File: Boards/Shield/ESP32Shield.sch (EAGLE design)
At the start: 29 parts, among them Q1 220mA/50V/3.5Ω, U1 5V

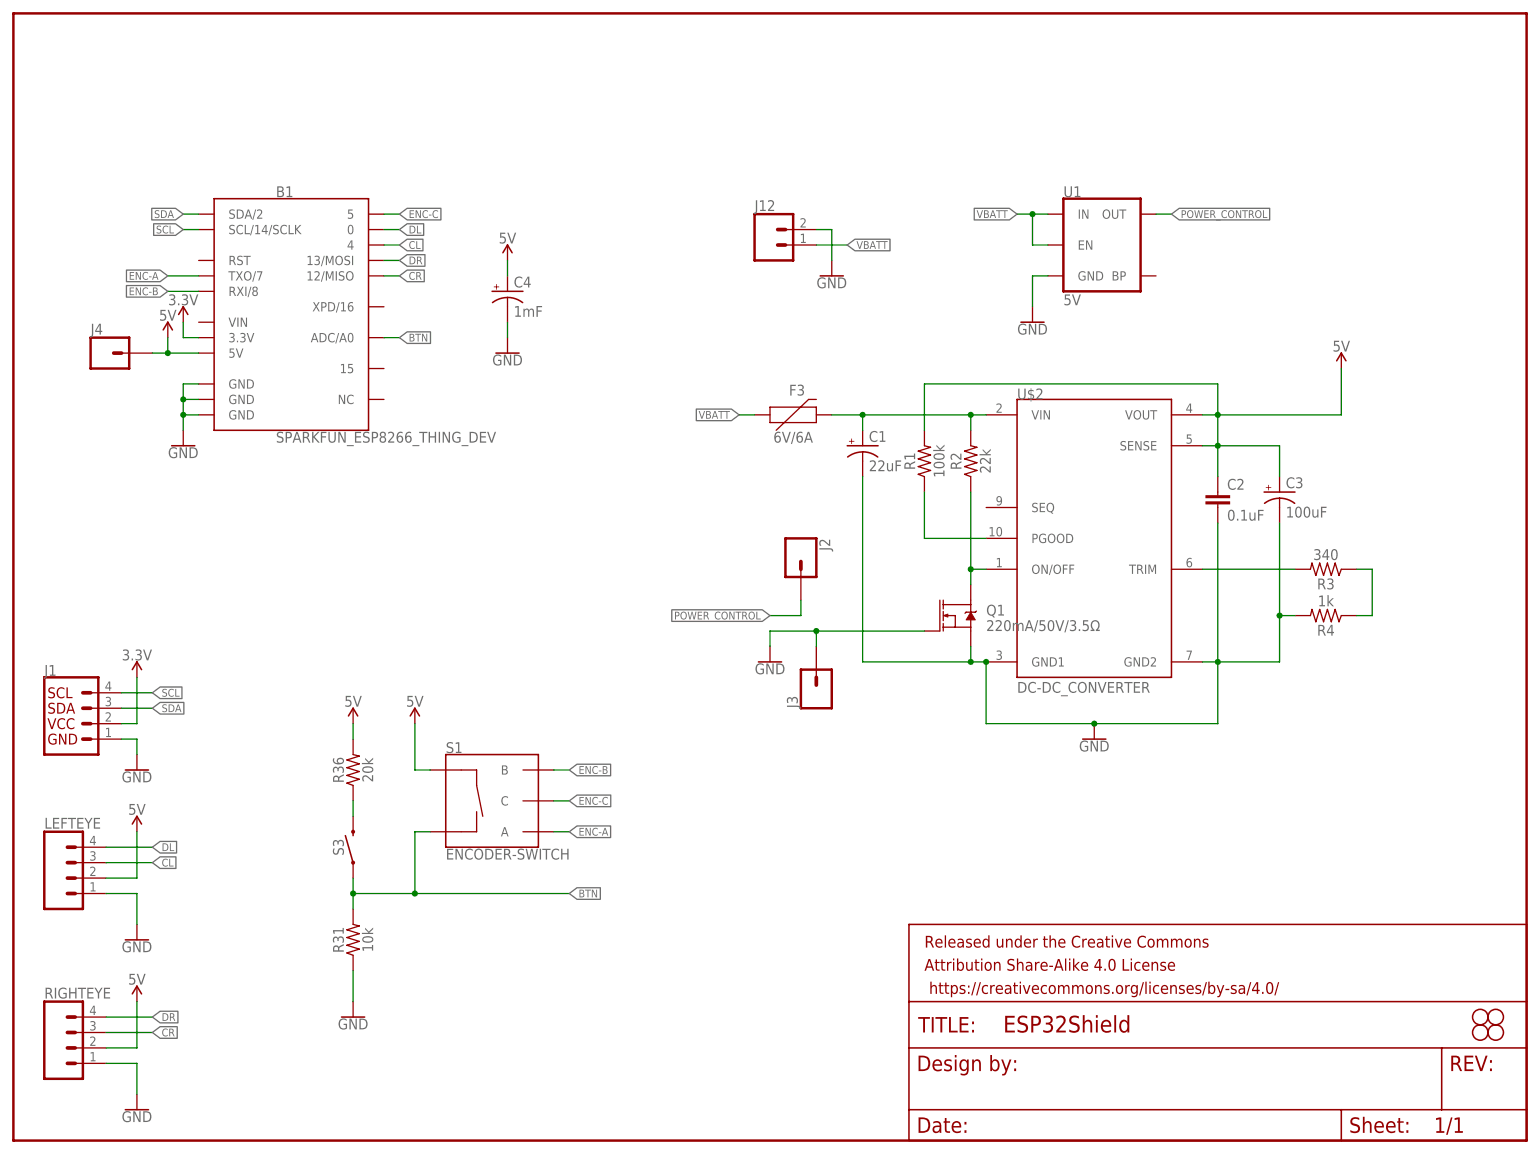
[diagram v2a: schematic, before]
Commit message: finished ESP32 Shield layout
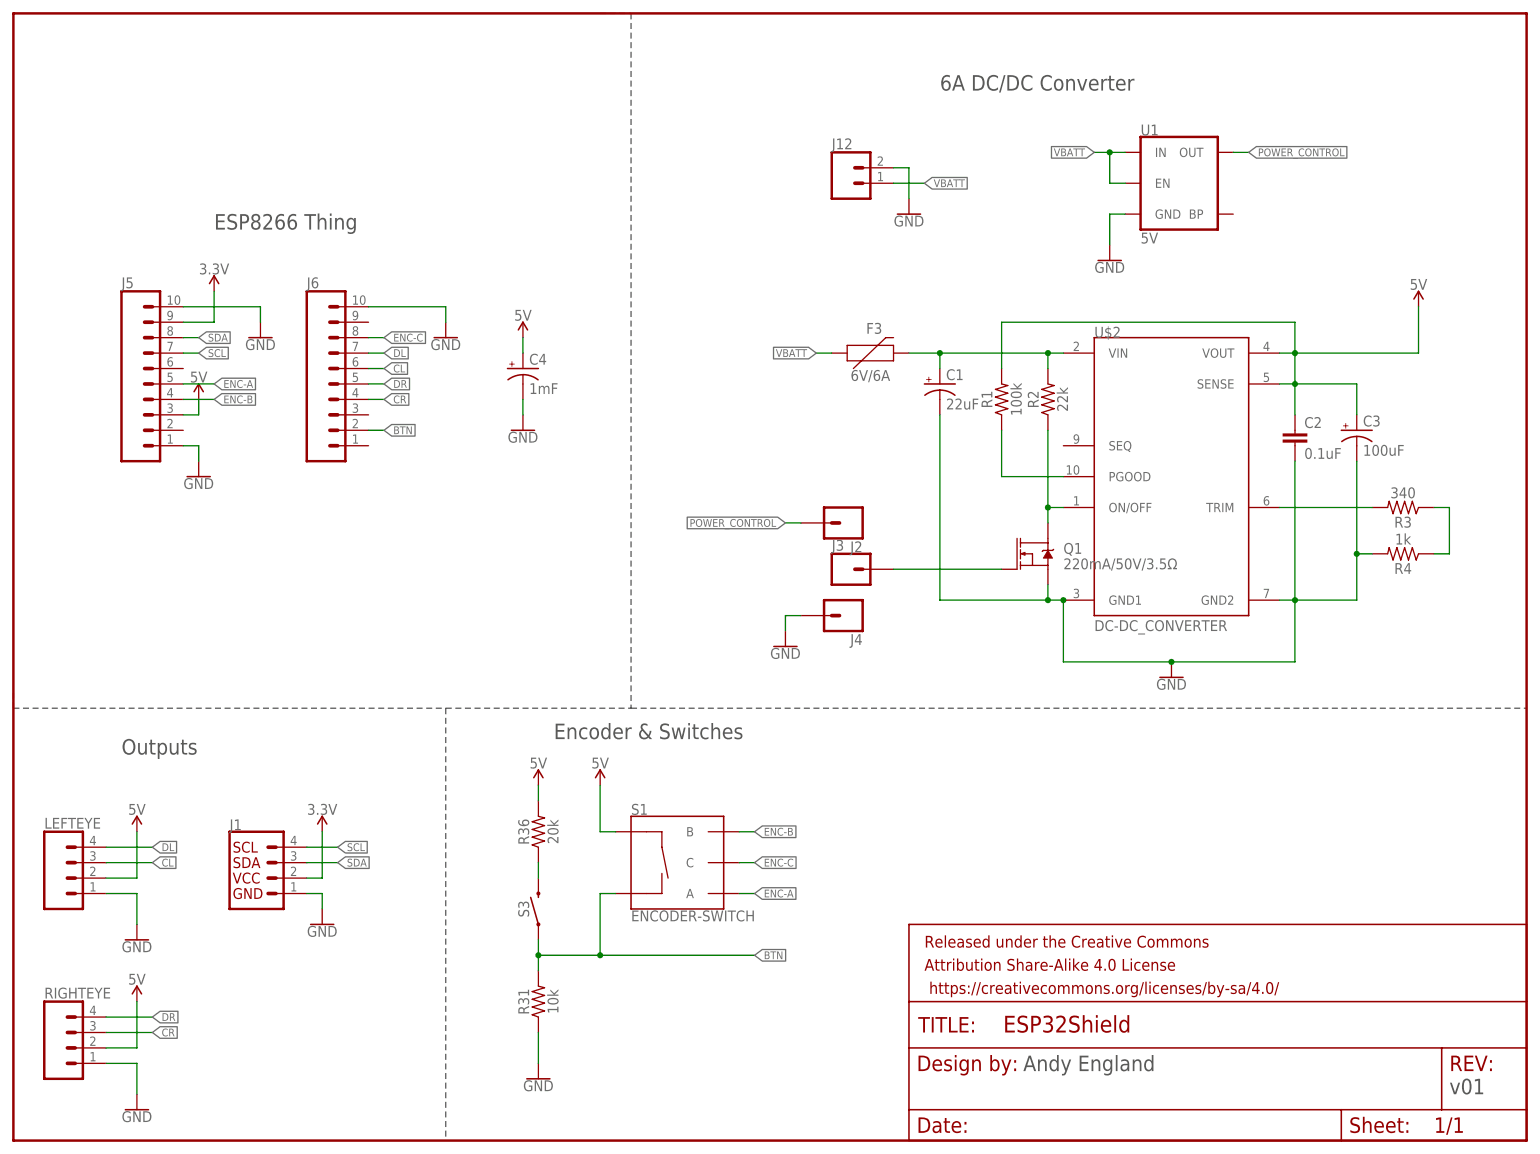
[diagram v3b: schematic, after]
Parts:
- removed B1: SPARKFUN_ESP8266_THING_DEV, SparkFun-Boards:SPARKFUN_ESP8266_THING_DEV
- removed H3, H4, H5, H6: STAND-OFFTIGHT, SparkFun-Hardware:STAND-OFFTIGHT
- added J5, J6: (no value), SparkFun-Connectors:CONN_10NO_SILK_PTH_FEMALE
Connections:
- new net N$1: J3.1, Q1.G
- net 3.3V: now also J5.9; no longer B1.3.3V
- net 5V: now also J5.3; no longer B1.5V, J4.1
- net BTN: now also J6.2; no longer B1.ADC/A0
- net CL: now also J6.6; no longer B1.4
- net CR: now also J6.4; no longer B1.12/MISO
- net DL: now also J6.7; no longer B1.0
- net DR: now also J6.5; no longer B1.13/MOSI
- net ENC-A: now also J5.5; no longer B1.TXO/7
- net ENC-B: now also J5.4; no longer B1.RXI/8
- net ENC-C: now also J6.8; no longer B1.5
- net GND: now also J4.1, J5.1, J5.10, J6.10; no longer B1.GND@1, B1.GND@2, B1.GND@3, J3.1, Q1.G
- net SCL: now also J5.7; no longer B1.SCL/14/SCLK
- net SDA: now also J5.8; no longer B1.SDA/2
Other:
- note added: "6A DC/DC Converter"
- note added: "Andy England"
- note added: "ESP8266 Thing"
- note added: "Encoder & Switches"
- note added: "Outputs"
- note added: "v01"
- moved on the sheet: C1, C2, C3, C4, F3, J1, J12, J2, J3, J4, Q1, R1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

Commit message: adding new pushbutton
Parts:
- S3: value MOMENTARY-SWITCH-SPST-SMD-4.5MM -> MOMENTARY-SWITCH-SPST-SMD-4.6X2.8MM; device SparkFun-Switches:MOMENTARY-SWITCH-SPST-SMD-4.5MM -> SparkFun-Switches:MOMENTARY-SWITCH-SPST-SMD-4.6X2.8MM
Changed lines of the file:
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@@
 <part name="GND20" library="SparkFun-PowerSymbols" deviceset="GND" device=""/>
 <part name="R36" library="SparkFun-Resistors" deviceset="20KOHM" device="-0603-1/10W-5%" value="20k"/>
-<part name="S3" library="SparkFun-Switches" deviceset="MOMENTARY-SWITCH-SPST" device="-SMD-4.5MM" value="MOMENTARY-SWITCH-SPST-SMD-4.5MM"/>
+<part name="S3" library="SparkFun-Switches" deviceset="MOMENTARY-SWITCH-SPST" device="-SMD-4.6X2.8MM" value="MOMENTARY-SWITCH-SPST-SMD-4.6X2.8MM"/>
 <part name="GND23" library="SparkFun-PowerSymbols" deviceset="GND" device=""/>
 <part name="U$2" library="SparkFun-IC-Power" deviceset="DC-DC_CONVERTER" device=""/>

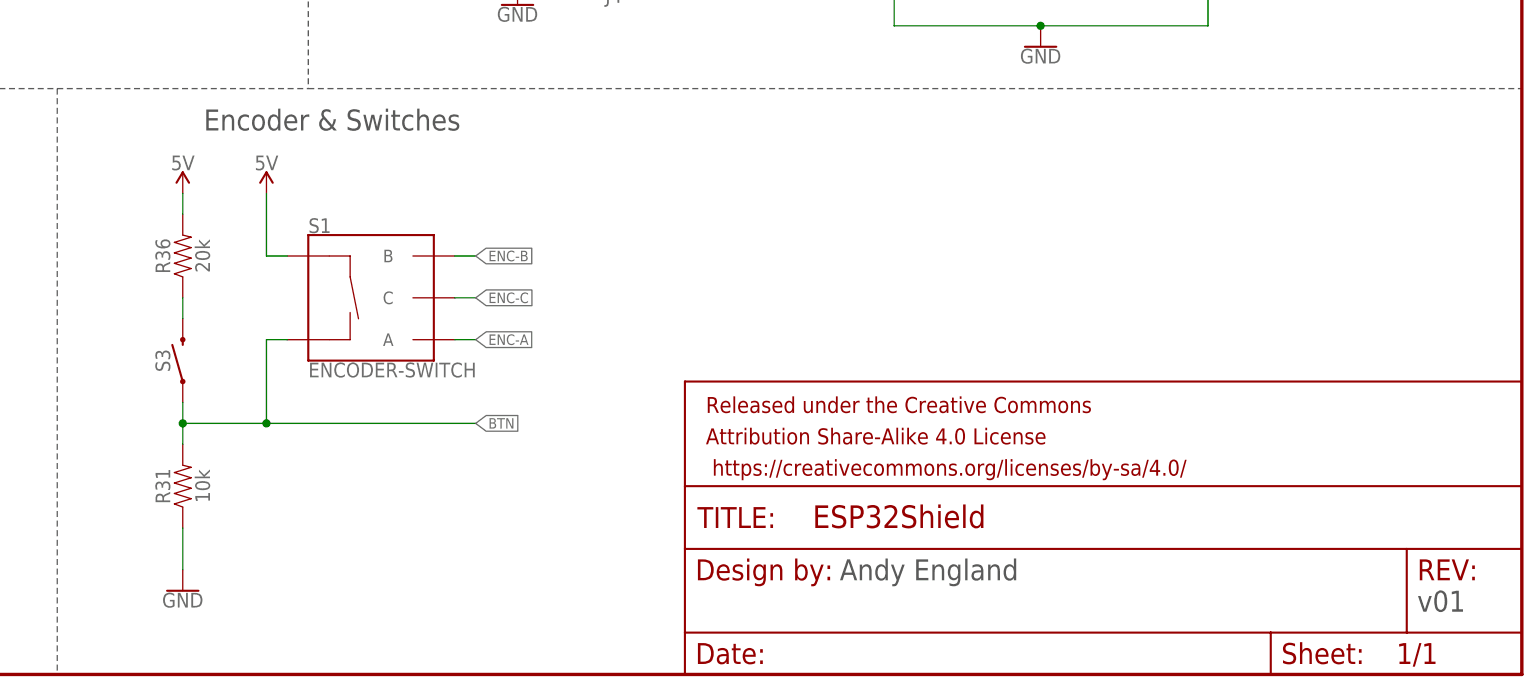
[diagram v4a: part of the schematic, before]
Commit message: updated resistors, silk
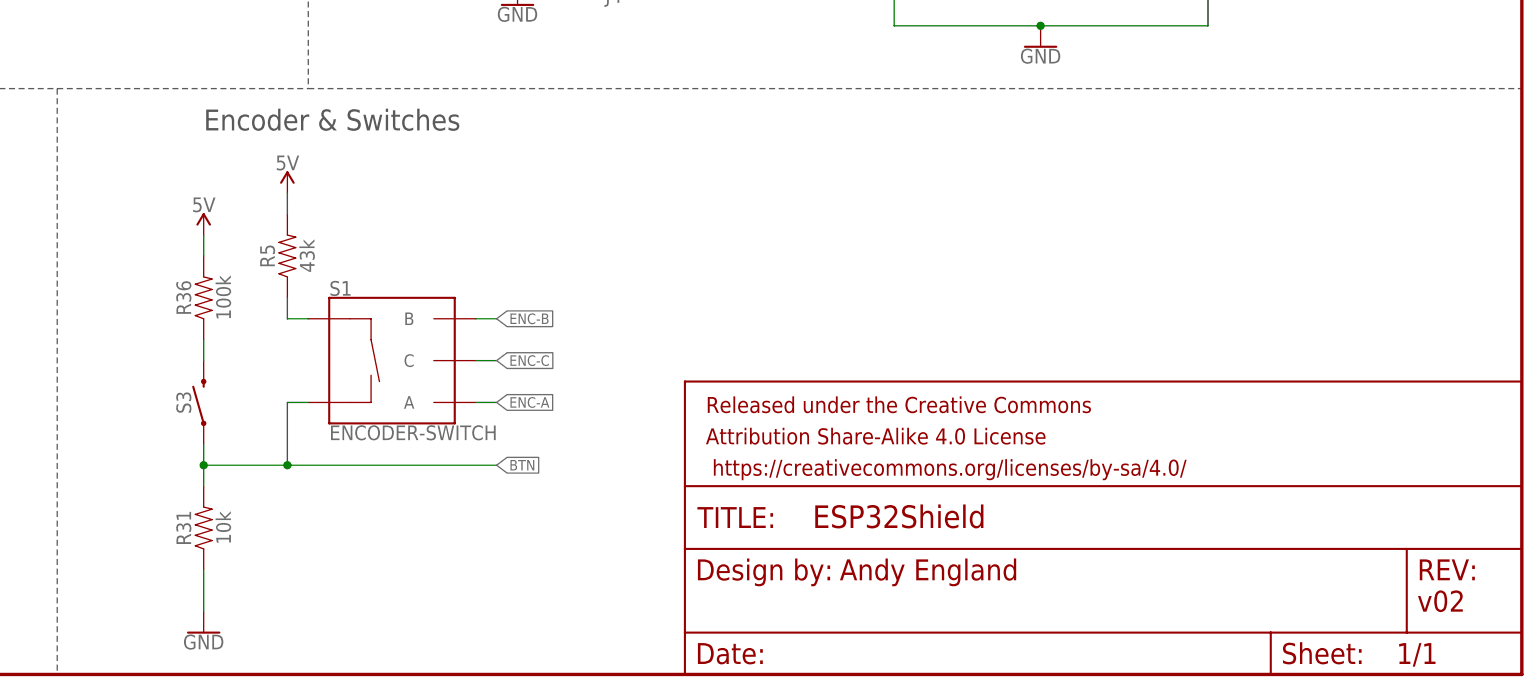
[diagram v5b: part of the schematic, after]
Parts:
- added R5: 43k, SparkFun-Resistors:43KOHM-0603-1/10W-1%
- R36: value 20k -> 100k; device SparkFun-Resistors:20KOHM-0603-1/10W-5% -> SparkFun-Resistors:100KOHM-0603-1/10W-1%
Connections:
- new net N$6: R5.1, S1.SW+
- net 5V: now also R5.2; no longer S1.SW+
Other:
- note added: "v02"
- note removed: "v01"
- moved on the sheet: R31, R36, S1, S3
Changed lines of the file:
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@@
 <part name="R31" library="SparkFun-Resistors" deviceset="10KOHM" device="-0603-1/10W-1%" value="10k"/>
 <part name="GND20" library="SparkFun-PowerSymbols" deviceset="GND" device=""/>
-<part name="R36" library="SparkFun-Resistors" deviceset="20KOHM" device="-0603-1/10W-5%" value="20k"/>
+<part name="R36" library="SparkFun-Resistors" deviceset="100KOHM" device="-0603-1/10W-1%" value="100k"/>
 <part name="S3" library="SparkFun-Switches" deviceset="MOMENTARY-SWITCH-SPST" device="-SMD-4.6X2.8MM" value="MOMENTARY-SWITCH-SPST-SMD-4.6X2.8MM"/>
 <part name="GND23" library="SparkFun-PowerSymbols" deviceset="GND" device=""/>
@@
 <part name="SUPPLY11" library="SparkFun-PowerSymbols" deviceset="3.3V" device=""/>
 <part name="GND9" library="SparkFun-PowerSymbols" deviceset="GND" device=""/>
+<part name="R5" library="SparkFun-Resistors" deviceset="43KOHM" device="-0603-1/10W-1%" value="43k"/>
 </parts>
 <sheets>
@@
 <text x="88.9" y="66.04" size="2.54" layer="97" font="vector">Encoder &amp; Switches</text>
 <text x="17.78" y="63.5" size="2.54" layer="97" font="vector">Outputs</text>
-<text x="166.116" y="11.43" size="2.54" layer="97" font="vector">Andy England</text>
-<text x="236.22" y="7.62" size="2.54" layer="97" font="vector">v01</text>
+<text x="166.116" y="11.43" size="2.54" layer="94" font="vector">Andy England</text>
+<text x="236.22" y="7.62" size="2.54" layer="94" font="vector">v02</text>
 </plain>
 <instances>
@@
 <instance part="RIGHTEYE" gate="G$1" x="10.16" y="15.24"/>
 <instance part="GND17" gate="1" x="20.32" y="5.08"/>
-<instance part="R31" gate="G$1" x="86.36" y="22.86" rot="R90"/>
-<instance part="GND20" gate="1" x="86.36" y="10.16"/>
-<instance part="R36" gate="G$1" x="86.36" y="50.8" rot="R90"/>
-<instance part="S3" gate="G$1" x="86.36" y="38.1" smashed="yes" rot="R90">
-<attribute name="NAME" x="84.836" y="38.1" size="1.778" layer="95" font="vector" rot="R90" align="bottom-center"/>
+<instance part="R31" gate="G$1" x="88.9" y="17.78" rot="R90"/>
+<instance part="GND20" gate="1" x="88.9" y="5.08"/>
+<instance part="R36" gate="G$1" x="88.9" y="45.72" rot="R90"/>
+<instance part="S3" gate="G$1" x="88.9" y="33.02" smashed="yes" rot="R90">
+<attribute name="NAME" x="87.376" y="33.02" size="1.778" layer="95" font="vector" rot="R90" align="bottom-center"/>
 </instance>
 <instance part="GND23" gate="1" x="147.32" y="152.4"/>
@@
 <instance part="SUPPLY3" gate="G$1" x="20.32" y="22.86"/>
 <instance part="SUPPLY4" gate="G$1" x="20.32" y="50.8"/>
-<instance part="SUPPLY5" gate="G$1" x="86.36" y="58.42"/>
-<instance part="S1" gate="G$1" x="109.22" y="45.72"/>
+<instance part="SUPPLY5" gate="G$1" x="88.9" y="53.34"/>
+<instance part="S1" gate="G$1" x="111.76" y="38.1"/>
 <instance part="J1" gate="G$1" x="40.64" y="43.18"/>
 <instance part="GND5" gate="1" x="50.8" y="35.56"/>
 <instance part="SUPPLY8" gate="G$1" x="50.8" y="50.8"/>
-<instance part="SUPPLY9" gate="G$1" x="96.52" y="58.42"/>
+<instance part="SUPPLY9" gate="G$1" x="99.06" y="58.42"/>
 <instance part="J2" gate="G$1" x="137.16" y="101.6" rot="R180"/>
 <instance part="J3" gate="G$1" x="137.16" y="93.98"/>
@@
 <instance part="SUPPLY11" gate="G$1" x="33.02" y="139.7"/>
 <instance part="GND9" gate="1" x="71.12" y="132.08"/>
+<instance part="R5" gate="G$1" x="99.06" y="50.8" rot="R90"/>
 </instances>
 <busses>
@@
 <pinref part="GND20" gate="1" pin="GND"/>
 <pinref part="R31" gate="G$1" pin="1"/>
-<wire x1="86.36" y1="12.7" x2="86.36" y2="17.78" width="0.1524" layer="91"/>
+<wire x1="88.9" y1="7.62" x2="88.9" y2="12.7" width="0.1524" layer="91"/>
 </segment>
 <segment>
@@
 <segment>
 <pinref part="R31" gate="G$1" pin="2"/>
-<wire x1="86.36" y1="27.94" x2="86.36" y2="30.48" width="0.1524" layer="91"/>
-<wire x1="86.36" y1="30.48" x2="86.36" y2="33.02" width="0.1524" layer="91"/>
-<junction x="86.36" y="30.48"/>
-<wire x1="86.36" y1="30.48" x2="96.52" y2="30.48" width="0.1524" layer="91"/>
-<label x="121.92" y="30.48" size="1.27" layer="95" xref="yes"/>
+<wire x1="88.9" y1="22.86" x2="88.9" y2="25.4" width="0.1524" layer="91"/>
+<wire x1="88.9" y1="25.4" x2="88.9" y2="27.94" width="0.1524" layer="91"/>
+<junction x="88.9" y="25.4"/>
+<wire x1="88.9" y1="25.4" x2="99.06" y2="25.4" width="0.1524" layer="91"/>
+<label x="124.46" y="25.4" size="1.27" layer="95" xref="yes"/>
 <pinref part="S3" gate="G$1" pin="1"/>
 <pinref part="S1" gate="G$1" pin="SW-"/>
-<wire x1="96.52" y1="30.48" x2="121.92" y2="30.48" width="0.1524" layer="91"/>
-<wire x1="99.06" y1="40.64" x2="96.52" y2="40.64" width="0.1524" layer="91"/>
-<wire x1="96.52" y1="40.64" x2="96.52" y2="30.48" width="0.1524" layer="91"/>
-<junction x="96.52" y="30.48"/>
+<wire x1="99.06" y1="25.4" x2="124.46" y2="25.4" width="0.1524" layer="91"/>
+<wire x1="101.6" y1="33.02" x2="99.06" y2="33.02" width="0.1524" layer="91"/>
+<wire x1="99.06" y1="33.02" x2="99.06" y2="25.4" width="0.1524" layer="91"/>
+<junction x="99.06" y="25.4"/>
 </segment>
 <segment>
@@
 <segment>
 <pinref part="R36" gate="G$1" pin="1"/>
-<wire x1="86.36" y1="45.72" x2="86.36" y2="43.18" width="0.1524" layer="91"/>
+<wire x1="88.9" y1="40.64" x2="88.9" y2="38.1" width="0.1524" layer="91"/>
 <pinref part="S3" gate="G$1" pin="2"/>
 </segment>
@@
 <segment>
 <pinref part="R36" gate="G$1" pin="2"/>
-<wire x1="86.36" y1="55.88" x2="86.36" y2="58.42" width="0.1524" layer="91"/>
+<wire x1="88.9" y1="50.8" x2="88.9" y2="53.34" width="0.1524" layer="91"/>
 <pinref part="SUPPLY5" gate="G$1" pin="5V"/>
-</segment>
-<segment>
-<pinref part="S1" gate="G$1" pin="SW+"/>
-<pinref part="SUPPLY9" gate="G$1" pin="5V"/>
-<wire x1="99.06" y1="50.8" x2="96.52" y2="50.8" width="0.1524" layer="91"/>
-<wire x1="96.52" y1="50.8" x2="96.52" y2="58.42" width="0.1524" layer="91"/>
 </segment>
 <segment>
@@
 <wire x1="30.48" y1="119.38" x2="30.48" y2="121.92" width="0.1524" layer="91"/>
 </segment>
+<segment>
+<pinref part="R5" gate="G$1" pin="2"/>
+<pinref part="SUPPLY9" gate="G$1" pin="5V"/>
+<wire x1="99.06" y1="58.42" x2="99.06" y2="55.88" width="0.1524" layer="91"/>
+</segment>
 </net>
 <net name="SDA" class="0">
@@
 <segment>
 <pinref part="S1" gate="G$1" pin="A"/>
-<wire x1="119.38" y1="40.64" x2="121.92" y2="40.64" width="0.1524" layer="91"/>
-<label x="121.92" y="40.64" size="1.27" layer="95" font="vector" xref="yes"/>
+<wire x1="121.92" y1="33.02" x2="124.46" y2="33.02" width="0.1524" layer="91"/>
+<label x="124.46" y="33.02" size="1.27" layer="95" font="vector" xref="yes"/>
 </segment>
 <segment>
@@
 <segment>
 <pinref part="S1" gate="G$1" pin="C"/>
-<wire x1="119.38" y1="45.72" x2="121.92" y2="45.72" width="0.1524" layer="91"/>
-<label x="121.92" y="45.72" size="1.27" layer="95" font="vector" xref="yes"/>
+<wire x1="121.92" y1="38.1" x2="124.46" y2="38.1" width="0.1524" layer="91"/>
+<label x="124.46" y="38.1" size="1.27" layer="95" font="vector" xref="yes"/>
 </segment>
 <segment>
@@
 <segment>
 <pinref part="S1" gate="G$1" pin="B"/>
-<wire x1="119.38" y1="50.8" x2="121.92" y2="50.8" width="0.1524" layer="91"/>
-<label x="121.92" y="50.8" size="1.27" layer="95" font="vector" xref="yes"/>
+<wire x1="121.92" y1="43.18" x2="124.46" y2="43.18" width="0.1524" layer="91"/>
+<label x="124.46" y="43.18" size="1.27" layer="95" font="vector" xref="yes"/>
 </segment>
 <segment>
@@
 </segment>
 </net>
+<net name="N$6" class="0">
+<segment>
+<pinref part="S1" gate="G$1" pin="SW+"/>
+<wire x1="101.6" y1="43.18" x2="99.06" y2="43.18" width="0.1524" layer="91"/>
+<pinref part="R5" gate="G$1" pin="1"/>
+<wire x1="99.06" y1="45.72" x2="99.06" y2="43.18" width="0.1524" layer="91"/>
+</segment>
+</net>
